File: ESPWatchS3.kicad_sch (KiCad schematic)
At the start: 116 parts

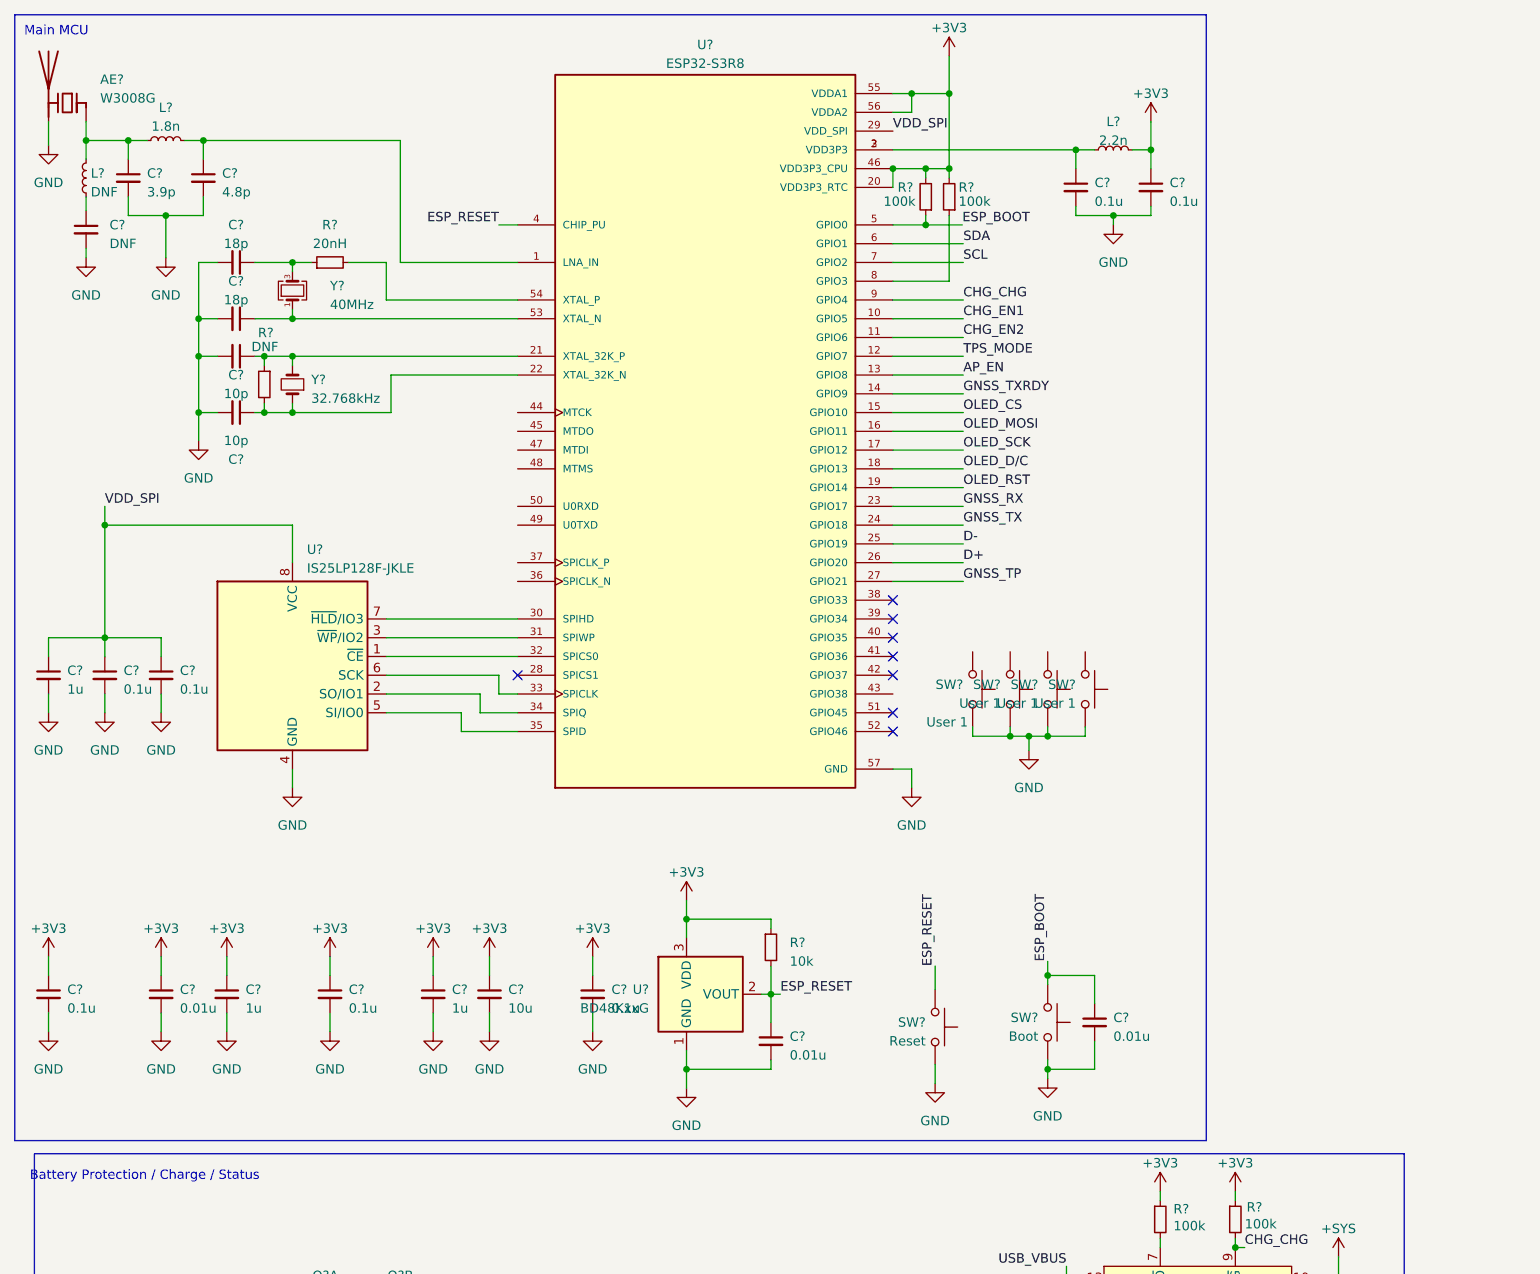
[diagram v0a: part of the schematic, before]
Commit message: Added buttons!
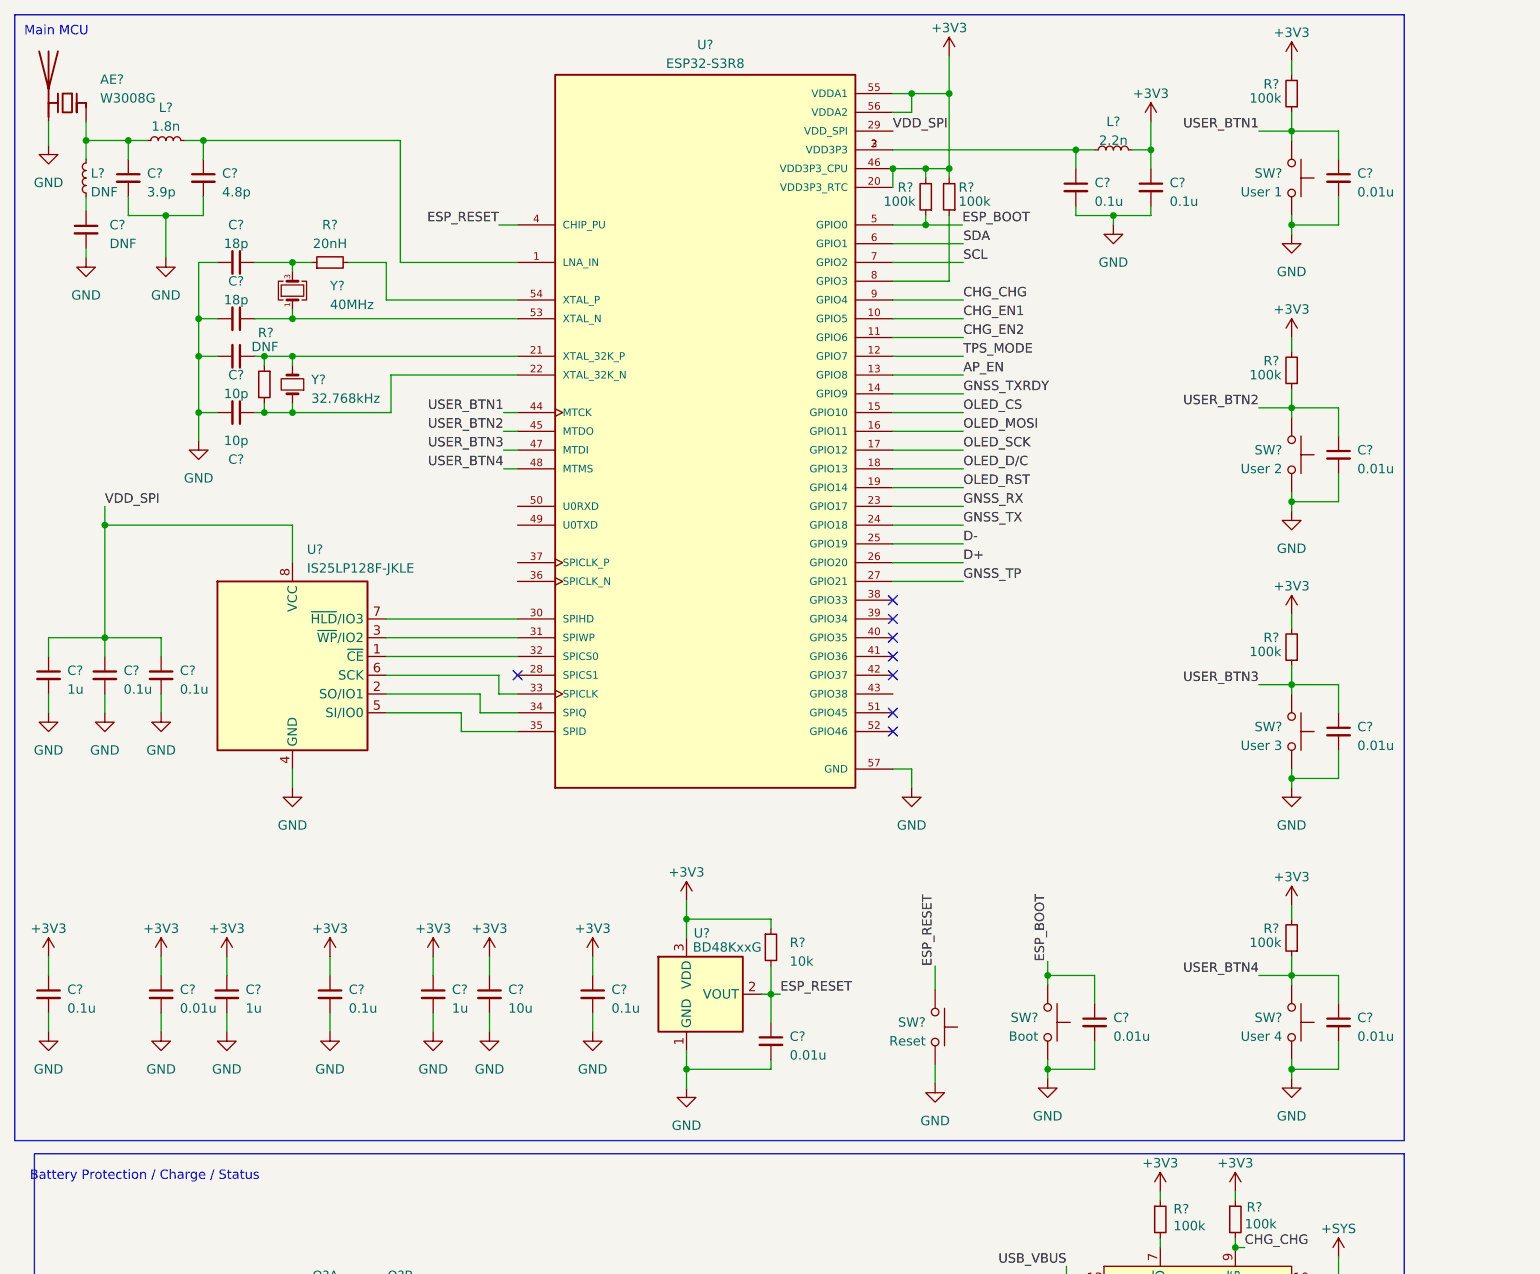
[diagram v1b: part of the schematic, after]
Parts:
- removed SW? (x4): User 1, WatchParts:PTS815SJM250SMTRLFS, symbol WatchParts:PTS815
- added C? (x4): 0.01u, symbol Device:C_Small
- added R? (x4): 100k, symbol Device:R_Small
- added SW?: User 3, WatchParts:PTS815SJM250SMTRLFS, symbol WatchParts:PTS815
- added SW?: User 1, WatchParts:PTS815SJM250SMTRLFS, symbol WatchParts:PTS815
- added SW?: User 4, WatchParts:PTS815SJM250SMTRLFS, symbol WatchParts:PTS815
- added SW?: User 2, WatchParts:PTS815SJM250SMTRLFS, symbol WatchParts:PTS815
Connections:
- net +3V3: now also R?.2, R?.2, R?.2, R?.2
- net EP: now also C?.2, C?.2, C?.2, C?.2, SW?.1, SW?.1, SW?.1, SW?.1, SW?.2, SW?.2, SW?.2, SW?.2
- net USER_BTN1: now reaches U?.44 (MTCK)
- net USER_BTN1: now also C?.1, R?.1, SW?.2, SW?.4
- net USER_BTN2: now reaches U?.45 (MTDO)
- net USER_BTN2: now also C?.1, R?.1, SW?.2, SW?.4
- net USER_BTN3: now reaches U?.47 (MTDI)
- net USER_BTN3: now also C?.1, R?.1, SW?.2, SW?.4
- net USER_BTN4: now reaches U?.48 (MTMS)
- net USER_BTN4: now also C?.1, R?.1, SW?.2, SW?.4

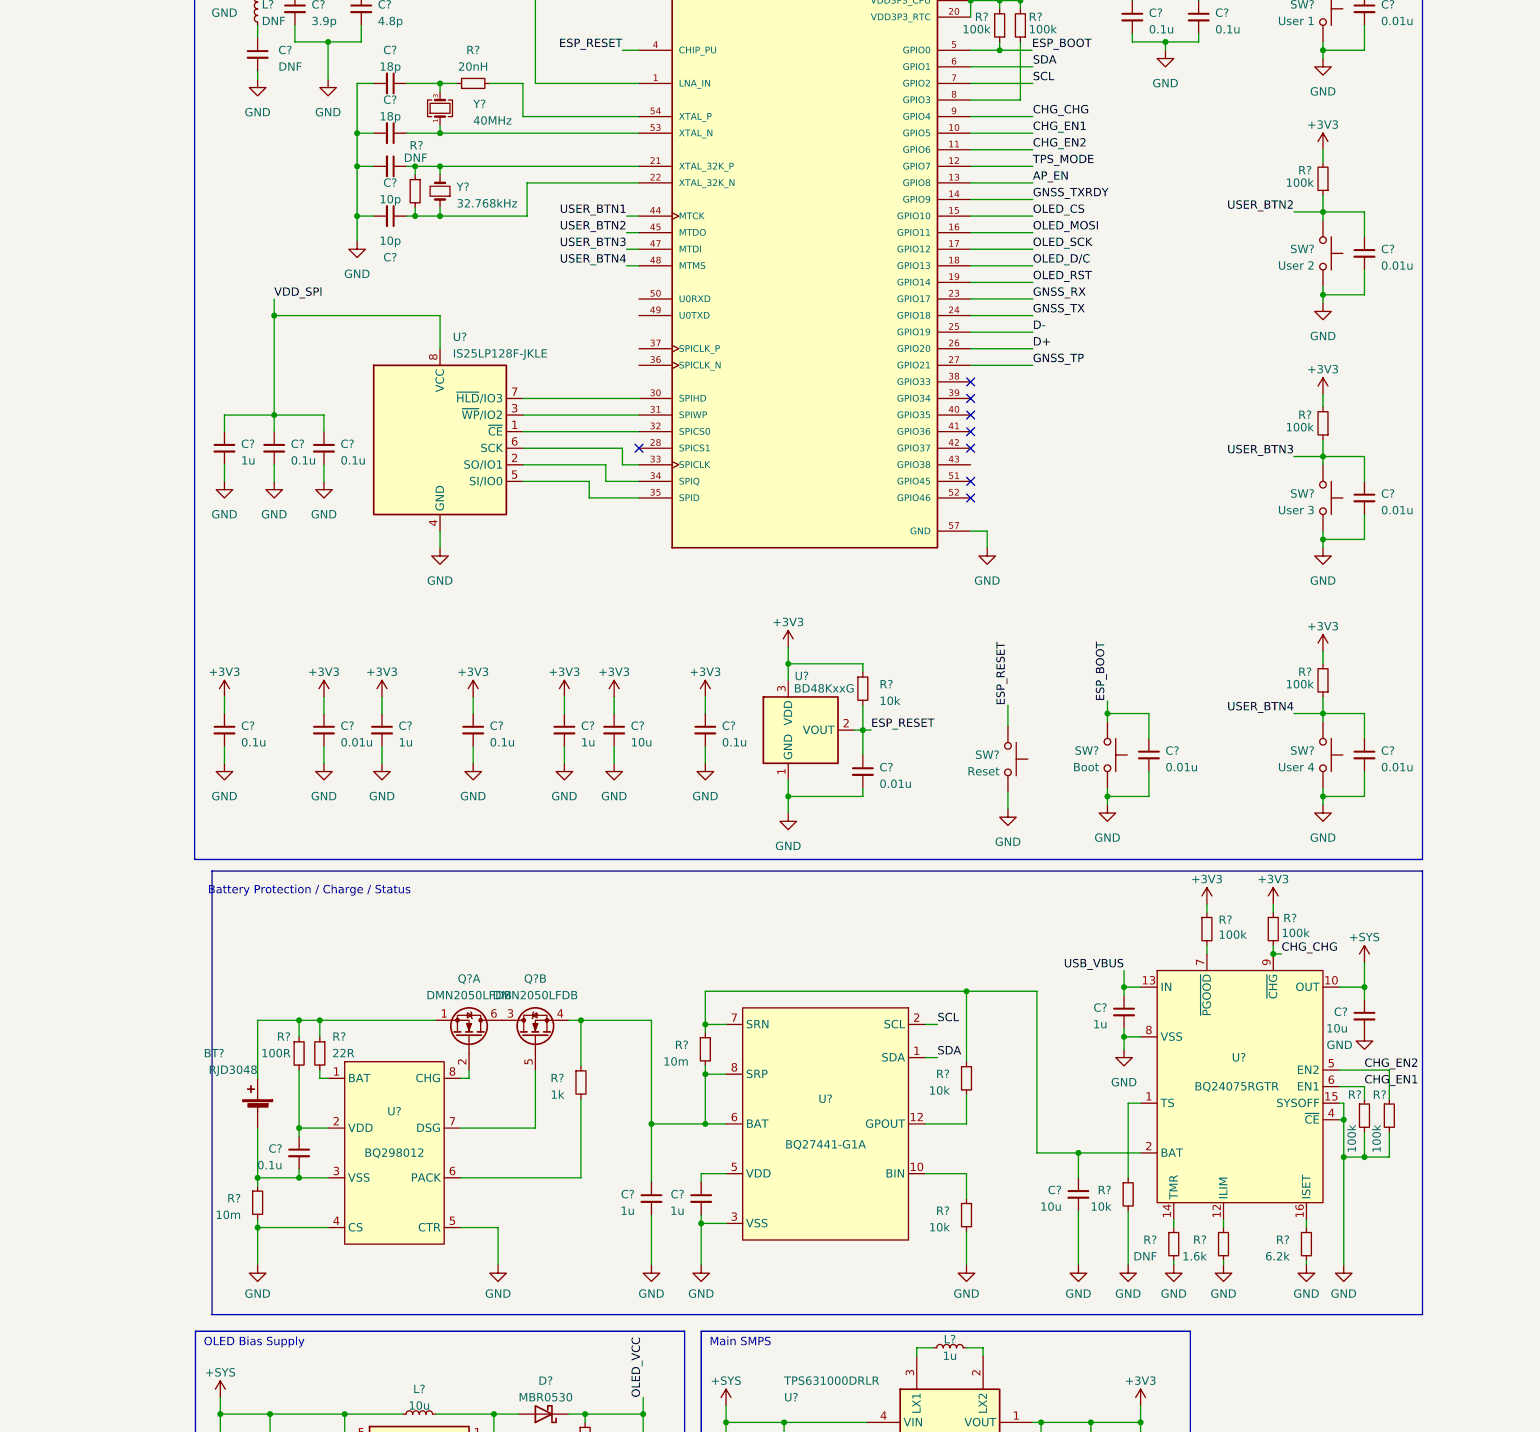
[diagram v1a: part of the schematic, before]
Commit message: Added Status LEDs, UART Debug
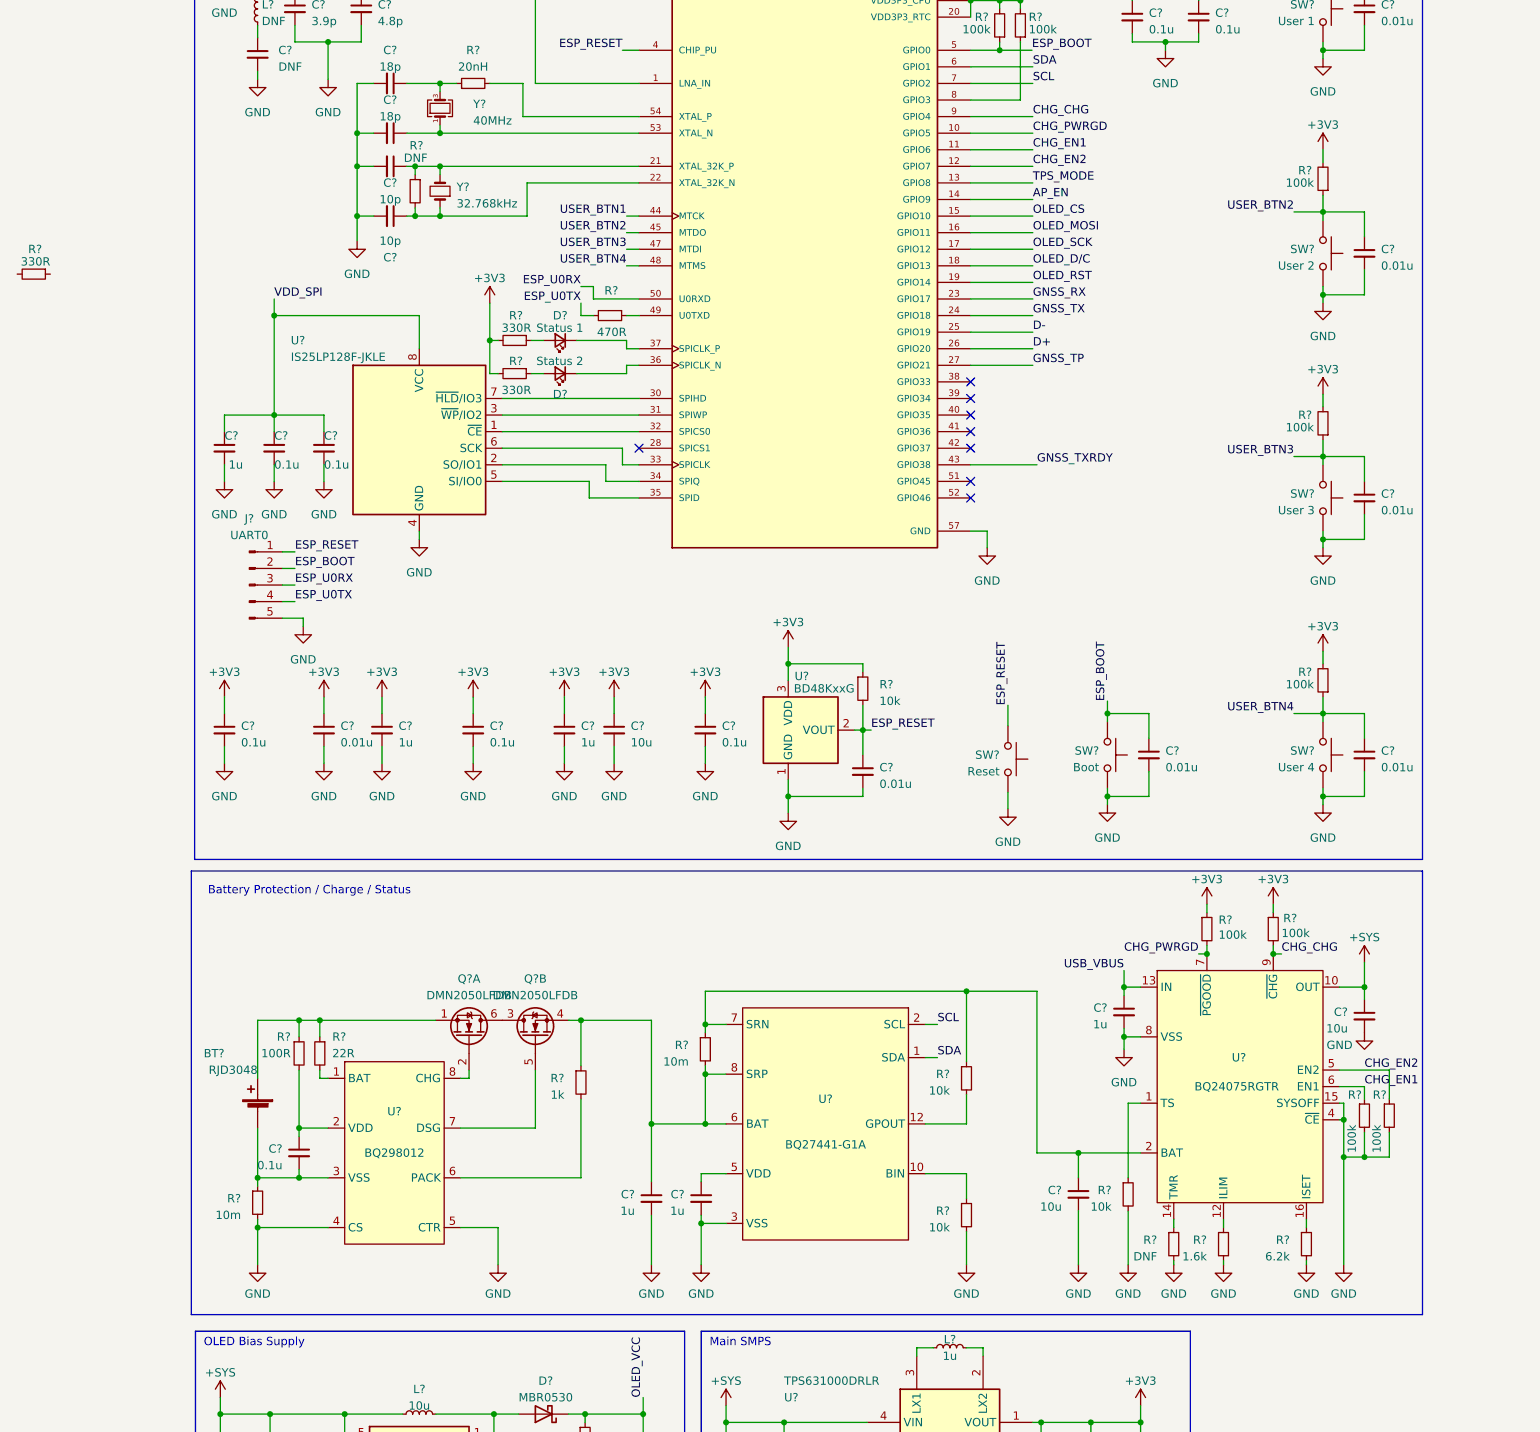
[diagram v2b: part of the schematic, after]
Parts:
- added D?: Status 1, symbol Device:LED_Small
- added D?: Status 2, symbol Device:LED_Small
- added J?: UART0, symbol Connector:Conn_01x05_Pin
- added R? (x3): 330R, symbol Device:R_Small
- added R?: 470R, symbol Device:R_Small
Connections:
- net +3V3: now also R?.2, R?.2
- net AP_EN: now also U?.14 (GPIO9); no longer U?.13 (GPIO8)
- net CHG_EN1: now also U?.11 (GPIO6); no longer U?.10 (GPIO5)
- net CHG_EN2: now also U?.12 (GPIO7); no longer U?.11 (GPIO6)
- net EP: now also J?.5 (Pin_5)
- net ESP_BOOT: now also J?.2 (Pin_2)
- net ESP_RESET: now also J?.1 (Pin_1)
- net GNSS_TXRDY: now also U?.43 (GPIO38); no longer U?.14 (GPIO9)
- net TPS_MODE: now also U?.13 (GPIO8); no longer U?.12 (GPIO7)
- net CHG_PWRGD: now reaches R?.2, U?.7 (~{PGOOD})
- net CHG_PWRGD: now also U?.10 (GPIO5)
- net at U?.36 (SPICLK_N): now also D?.1 (K)
- net at U?.37 (SPICLK_P): now also D?.1 (K)
- net at U?.49 (U0TXD): now also R?.1
- net ESP_U0RX: now reaches U?.50 (U0RXD)
- net ESP_U0RX: now also J?.3 (Pin_3)
- new net: D?.2 (A), R?.1 (x2)
- new net ESP_U0TX: J?.4 (Pin_4), R?.2
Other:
- moved on the sheet: U?

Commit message: Mostly finished schematic layout
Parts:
- removed R?: 330R, symbol Device:R_Small
- added R? (x2): 2.2k, symbol Device:R_Small
- added TP?: VMAIN, symbol Connector:TestPoint_Small
- added TP?: VOLED, symbol Connector:TestPoint_Small
- added TP?: VBATT, symbol Connector:TestPoint_Small
- added TP?: VSYS, symbol Connector:TestPoint_Small
- added TP?: VUSB, symbol Connector:TestPoint_Small
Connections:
- net +3V3: now also R?.1, R?.1, TP?.1
- net +SYS: now also TP?.1
- net BAT: now also TP?.1
- net OLED_VCC: now also TP?.1
- net SCL: now also R?.2
- net SDA: now also R?.2
- net USB_VBUS: now also TP?.1
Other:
- moved on the sheet: ANT?, C?, FL?, J?, L?, R?, TP?, U?, Y?
